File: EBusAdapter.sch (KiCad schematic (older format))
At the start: 20 parts

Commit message: Initial hardware
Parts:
- removed U?: 78L05, symbol 78L05
- added C3: CP, Capacitors_ThroughHole:C_Radial_D8_L11.5_P3.5, symbol CP
- added C4: 680nF, Capacitors_ThroughHole:C_Disc_D6_P5, symbol C_Small
- added CON1: BARREL_JACK, Connect:BARREL_JACK, symbol BARREL_JACK
- added D6: 1N4001, Diodes_ThroughHole:Diode_DO-35_SOD27_Horizontal_RM10, symbol D_Small
- added P2: CONN_01X06, Socket_Strips:Socket_Strip_Straight_1x06, symbol CONN_01X06
- added P3, P4: CONN_01X04, Connectors_Molex:Molex_KK-6410-04_04x2.54mm_Straight, symbol CONN_01X04
- added R5: R, Resistors_ThroughHole:Resistor_Horizontal_RM10mm, symbol R
- added U2: LM78L05ACZ, TO_SOT_Packages_THT:TO-92_Inline_Wide, symbol LM78L05ACZ
- added U4: PHOTON, particle-boards:PHOTON, symbol PHOTON
- added U5: LM7805CT, TO_SOT_Packages_THT:TO-220_Neutral123_Horizontal_LargePads, symbol LM7805CT
- C1, C2: renamed from C?; footprint (none) -> Capacitors_ThroughHole:C_Disc_D6_P5
- D1, D2, D3, D4: renamed from D?; footprint (none) -> Diodes_ThroughHole:Diode_DO-35_SOD27_Horizontal_RM10
- D5: renamed from D?; footprint (none) -> LEDs:LED-5MM
- P1: renamed from P?; footprint (none) -> Connectors_Phoenix:PhoenixContact_MC-G_02x5.08mm_Angled
- Q1: renamed from Q?; footprint TO-92 -> TO_SOT_Packages_THT:TO-92_Inline_Wide
- R1: renamed from R?; value R -> 4.7k; footprint (none) -> Resistors_ThroughHole:Resistor_Horizontal_RM10mm
- R2, R3, R4: renamed from R?; footprint (none) -> Resistors_ThroughHole:Resistor_Horizontal_RM10mm
- RV1: renamed from RV?; footprint (none) -> ebus-adapter:TRIMMER_5_10
- U1: renamed from U?; footprint (none) -> Housings_DIP:DIP-14_W7.62mm
- U3: renamed from U?; footprint SO-8 -> Housings_SOIC:SOIC-8_3.9x4.9mm_Pitch1.27mm
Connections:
- net VDD is gone; now on net GND: U1.14 (VDD), U1.14 (VDD), U1.14 (VDD), U1.14 (VDD)
- net VSS is gone; now on net VCC: U1.7 (VSS), U1.7 (VSS), U1.7 (VSS), U1.7 (VSS)
- net GND: now also U1.12, U1.13, U2.2 (GND); no longer U1.1, U1.2
- net VCC: now also U1.5, U1.8, U2.1 (OUT); no longer U1.1, U1.1
- net at C1.1, D4.1 (K): now also U2.3 (IN)
- net at RV1.2: now also U1.6; no longer U1.2
- net at U3.3 (VIB): now also U1.10; no longer U1.3
- net GNDD: now reaches U3.5 (GND2)
- net GNDD: now also C3.2, C4.2, CON1.2, P2.1 (P1), P3.1 (P1), P4.1 (P1), U4.2 (GND), U5.2 (GND)
- net RX: now reaches U3.6 (VOB)
- net RX: now also P2.5 (P5), U4.4 (RX)
- net TX: now reaches U3.7 (VIA)
- net TX: now also P2.4 (P4), U4.3 (TX)
- net +3V3: now reaches U3.8 (VDD2)
- net +3V3: now also P2.3 (P3), P3.4 (P4), P4.4 (P4), R5.1, U4.24 (3.3V)
- new net: P3.2 (P2), P4.2 (P2), R5.2, U4.16 (D3)
- new net: CON1.1, D6.2 (A)
- new net: U1.4, U1.9
- new net: C3.1, D6.1 (K), U5.1 (IN)
- new net +5V: C4.1, U4.1 (VIN), U5.3 (OUT)
- no-connect marks 0 -> 23

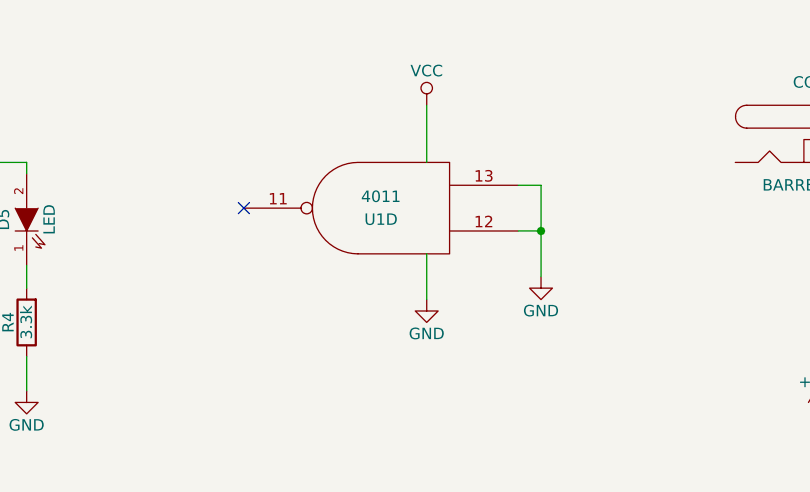
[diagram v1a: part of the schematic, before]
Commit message: Fix CD4011 power supply (was inverted) - added logo
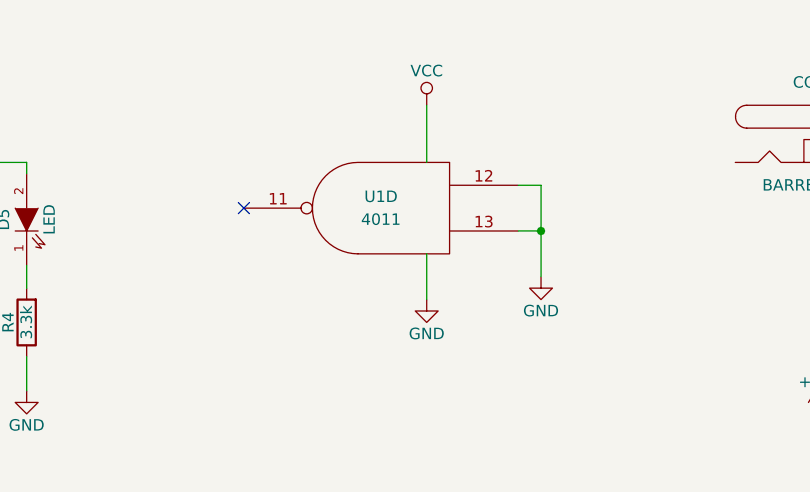
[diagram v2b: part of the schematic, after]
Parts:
- U1: footprint Housings_DIP:DIP-14_W7.62mm -> Housings_DIP:DIP-14_W7.62mm_LongPads
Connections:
- net GND: now also U1.7 (VSS), U1.7 (VSS), U1.7 (VSS), U1.7 (VSS); no longer U1.14 (VDD), U1.14 (VDD), U1.14 (VDD), U1.14 (VDD)
- net VCC: now also U1.14 (VDD), U1.14 (VDD), U1.14 (VDD), U1.14 (VDD); no longer U1.7 (VSS), U1.7 (VSS), U1.7 (VSS), U1.7 (VSS)
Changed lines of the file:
@@
 F 0 "U1" H 3150 3450 50  0000 C CNN
 F 1 "4011" H 3150 3350 50  0000 C CNN
-F 2 "Housings_DIP:DIP-14_W7.62mm" H 3150 3400 60  0001 C CNN
+F 2 "Housings_DIP:DIP-14_W7.62mm_LongPads" H 3150 3400 60  0001 C CNN
 F 3 "" H 3150 3400 60  0001 C CNN
 	2    3150 3400
@@
 F 0 "U1" H 4550 3450 50  0000 C CNN
 F 1 "4011" H 4550 3350 50  0000 C CNN
-F 2 "Housings_DIP:DIP-14_W7.62mm" H 4550 3400 60  0001 C CNN
+F 2 "Housings_DIP:DIP-14_W7.62mm_LongPads" H 4550 3400 60  0001 C CNN
 F 3 "" H 4550 3400 60  0001 C CNN
 	3    4550 3400
@@
 F 0 "U1" H 1500 4150 50  0000 C CNN
 F 1 "4011" H 1500 4050 50  0000 C CNN
-F 2 "Housings_DIP:DIP-14_W7.62mm" H 1500 4100 60  0001 C CNN
+F 2 "Housings_DIP:DIP-14_W7.62mm_LongPads" H 1500 4100 60  0001 C CNN
 F 3 "" H 1500 4100 60  0001 C CNN
 	1    1500 4100
@@
 F 0 "U1" H 5800 1650 50  0000 C CNN
 F 1 "4011" H 5800 1550 50  0000 C CNN
-F 2 "Housings_DIP:DIP-14_W7.62mm" H 5800 1600 60  0001 C CNN
+F 2 "Housings_DIP:DIP-14_W7.62mm_LongPads" H 5800 1600 60  0001 C CNN
 F 3 "" H 5800 1600 60  0001 C CNN
 	4    5800 1600
-	-1   0    0    1
+	-1   0    0    -1
 $EndComp
 Wire Wire Line
@@
 	7700 2700 7700 2800
 $Comp
-L GNDD #PWR017
+L GNDD #PWR015
 U 1 1 584EC984
 P 7700 2800
-F 0 "#PWR017" H 7700 2550 50  0001 C CNN
+F 0 "#PWR015" H 7700 2550 50  0001 C CNN
 F 1 "GNDD" H 7700 2650 50  0000 C CNN
 F 2 "" H 7700 2800 50  0000 C CNN
@@
 	7900 2800 7900 2500
 $Comp
-L +3.3V #PWR018
+L +3.3V #PWR016
 U 1 1 584ECC3C
 P 7900 2500
-F 0 "#PWR018" H 7900 2350 50  0001 C CNN
+F 0 "#PWR016" H 7900 2350 50  0001 C CNN
 F 1 "+3.3V" H 7900 2640 50  0000 C CNN
 F 2 "" H 7900 2500 50  0000 C CNN
@@
 $EndComp
 $Comp
-L +3.3V #PWR019
+L +3.3V #PWR017
 U 1 1 584ECC99
 P 10300 3100
-F 0 "#PWR019" H 10300 2950 50  0001 C CNN
+F 0 "#PWR017" H 10300 2950 50  0001 C CNN
 F 1 "+3.3V" H 10300 3240 50  0000 C CNN
 F 2 "" H 10300 3100 50  0000 C CNN
@@
 $EndComp
 $Comp
-L +3.3V #PWR020
+L +3.3V #PWR018
 U 1 1 584ECF38
 P 10000 4100
-F 0 "#PWR020" H 10000 3950 50  0001 C CNN
+F 0 "#PWR018" H 10000 3950 50  0001 C CNN
 F 1 "+3.3V" H 10000 4240 50  0000 C CNN
 F 2 "" H 10000 4100 50  0000 C CNN
@@
 	10000 4300 10150 4300
 $Comp
-L GNDD #PWR021
+L GNDD #PWR019
 U 1 1 584ED098
 P 10000 4700
-F 0 "#PWR021" H 10000 4450 50  0001 C CNN
+F 0 "#PWR019" H 10000 4450 50  0001 C CNN
 F 1 "GNDD" H 10000 4550 50  0000 C CNN
 F 2 "" H 10000 4700 50  0000 C CNN
@@
 $EndComp
 $Comp
-L GNDD #PWR022
+L GNDD #PWR020
 U 1 1 584ED5F3
 P 10000 5600
-F 0 "#PWR022" H 10000 5350 50  0001 C CNN
+F 0 "#PWR020" H 10000 5350 50  0001 C CNN
 F 1 "GNDD" H 10000 5450 50  0000 C CNN
 F 2 "" H 10000 5600 50  0000 C CNN
@@
 $EndComp
 $Comp
-L +3.3V #PWR023
+L +3.3V #PWR021
 U 1 1 584ED64F
 P 10000 5100
-F 0 "#PWR023" H 10000 4950 50  0001 C CNN
+F 0 "#PWR021" H 10000 4950 50  0001 C CNN
 F 1 "+3.3V" H 10000 5240 50  0000 C CNN
 F 2 "" H 10000 5100 50  0000 C CNN
@@
 Connection ~ 8200 1200
 $Comp
-L PWR_FLAG #FLG024
+L PWR_FLAG #FLG022
 U 1 1 584EFDAE
 P 8500 1500
-F 0 "#FLG024" H 8500 1595 50  0001 C CNN
+F 0 "#FLG022" H 8500 1595 50  0001 C CNN
 F 1 "PWR_FLAG" H 8500 1680 50  0000 C CNN
 F 2 "" H 8500 1500 50  0000 C CNN
@@
 	6000 1800 6000 2000
 $Comp
-L GND #PWR025
+L GND #PWR023
 U 1 1 584F0701
 P 6000 2000
-F 0 "#PWR025" H 6000 1750 50  0001 C CNN
+F 0 "#PWR023" H 6000 1750 50  0001 C CNN
 F 1 "GND" H 6000 1850 50  0000 C CNN
 F 2 "" H 6000 2000 50  0000 C CNN
@@
 $EndComp
 $Comp
-L VCC #PWR026
+L VCC #PWR024
 U 1 1 584F0766
 P 6000 1150
-F 0 "#PWR026" H 6000 1000 50  0001 C CNN
+F 0 "#PWR024" H 6000 1000 50  0001 C CNN
 F 1 "VCC" H 6000 1300 50  0000 C CNN
 F 2 "" H 6000 1150 50  0000 C CNN
@@
 $EndComp
 $Comp
-L +3.3V #PWR027
+L +3.3V #PWR025
 U 1 1 584FD72C
 P 6800 3200
-F 0 "#PWR027" H 6800 3050 50  0001 C CNN
+F 0 "#PWR025" H 6800 3050 50  0001 C CNN
 F 1 "+3.3V" H 6800 3340 50  0000 C CNN
 F 2 "" H 6800 3200 50  0000 C CNN
@@
 $EndComp
 $Comp
-L +3.3V #PWR028
+L +3.3V #PWR026
 U 1 1 584FD866
 P 7000 4600
-F 0 "#PWR028" H 7000 4450 50  0001 C CNN
+F 0 "#PWR026" H 7000 4450 50  0001 C CNN
 F 1 "+3.3V" H 7000 4740 50  0000 C CNN
 F 2 "" H 7000 4600 50  0000 C CNN
@@
 $EndComp
 $Comp
-L GNDD #PWR029
+L GNDD #PWR027
 U 1 1 584EB9FF
 P 9500 1800
-F 0 "#PWR029" H 9500 1550 50  0001 C CNN
+F 0 "#PWR027" H 9500 1550 50  0001 C CNN
 F 1 "GNDD" H 9500 1650 50  0000 C CNN
 F 2 "" H 9500 1800 50  0000 C CNN
@@
 Connection ~ 9000 1200
 $Comp
-L +5V #PWR?
+L +5V #PWR028
 U 1 1 584FF1CE
 P 10200 1100
-F 0 "#PWR?" H 10200 950 50  0001 C CNN
+F 0 "#PWR028" H 10200 950 50  0001 C CNN
 F 1 "+5V" H 10200 1240 50  0000 C CNN
 F 2 "" H 10200 1100 50  0000 C CNN
@@
 $EndComp
 $Comp
-L +5V #PWR?
+L +5V #PWR029
 U 1 1 584FF492
 P 7700 2500
-F 0 "#PWR?" H 7700 2350 50  0001 C CNN
+F 0 "#PWR029" H 7700 2350 50  0001 C CNN
 F 1 "+5V" H 7700 2640 50  0000 C CNN
 F 2 "" H 7700 2500 50  0000 C CNN
